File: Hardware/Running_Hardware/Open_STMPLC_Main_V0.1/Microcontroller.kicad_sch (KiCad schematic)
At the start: 73 parts, among them J1 Conn_02x08_Odd_Even, J12 USB C, J2 USB C, J3 Conn_01x04, SW1 Switch_6x6, U1 STM32F407IGTx, U3 TPS3430WDRC, U4 CH340C, Y1 48MHz, Y2 32.768kHz

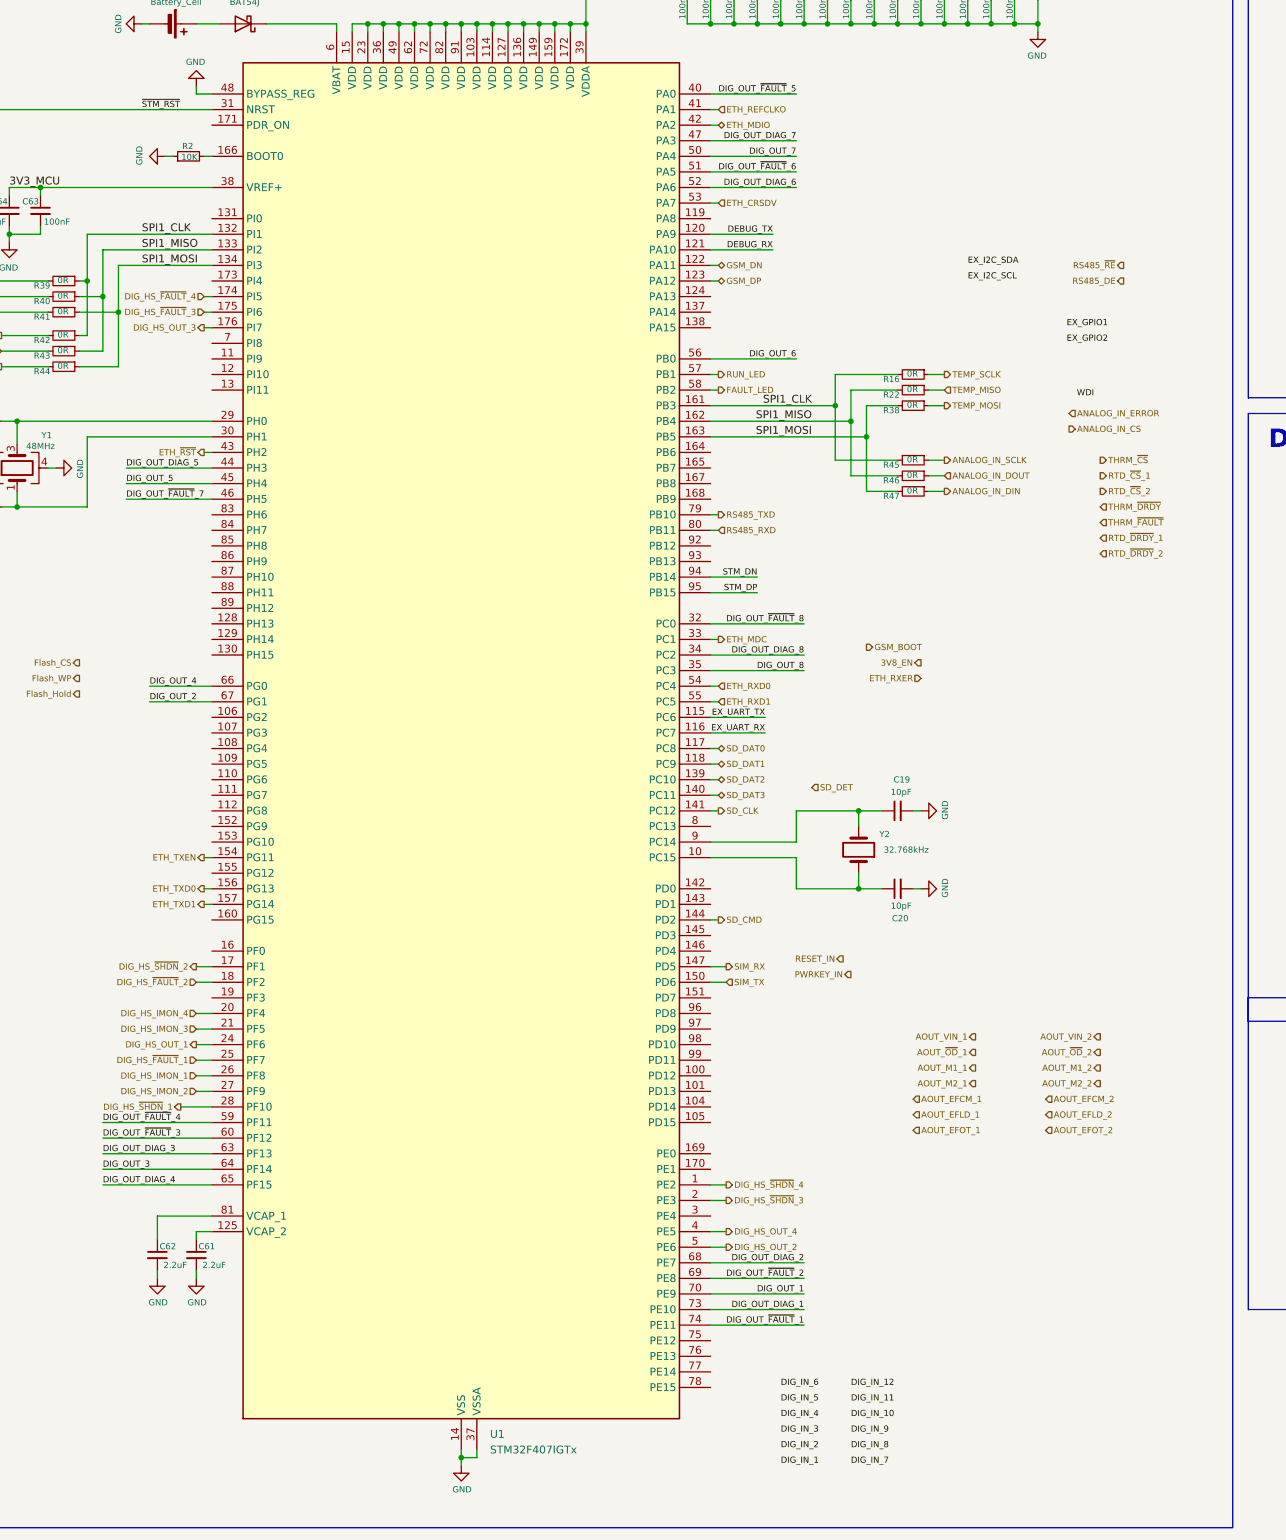
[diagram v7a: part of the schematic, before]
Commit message: Pin mapping
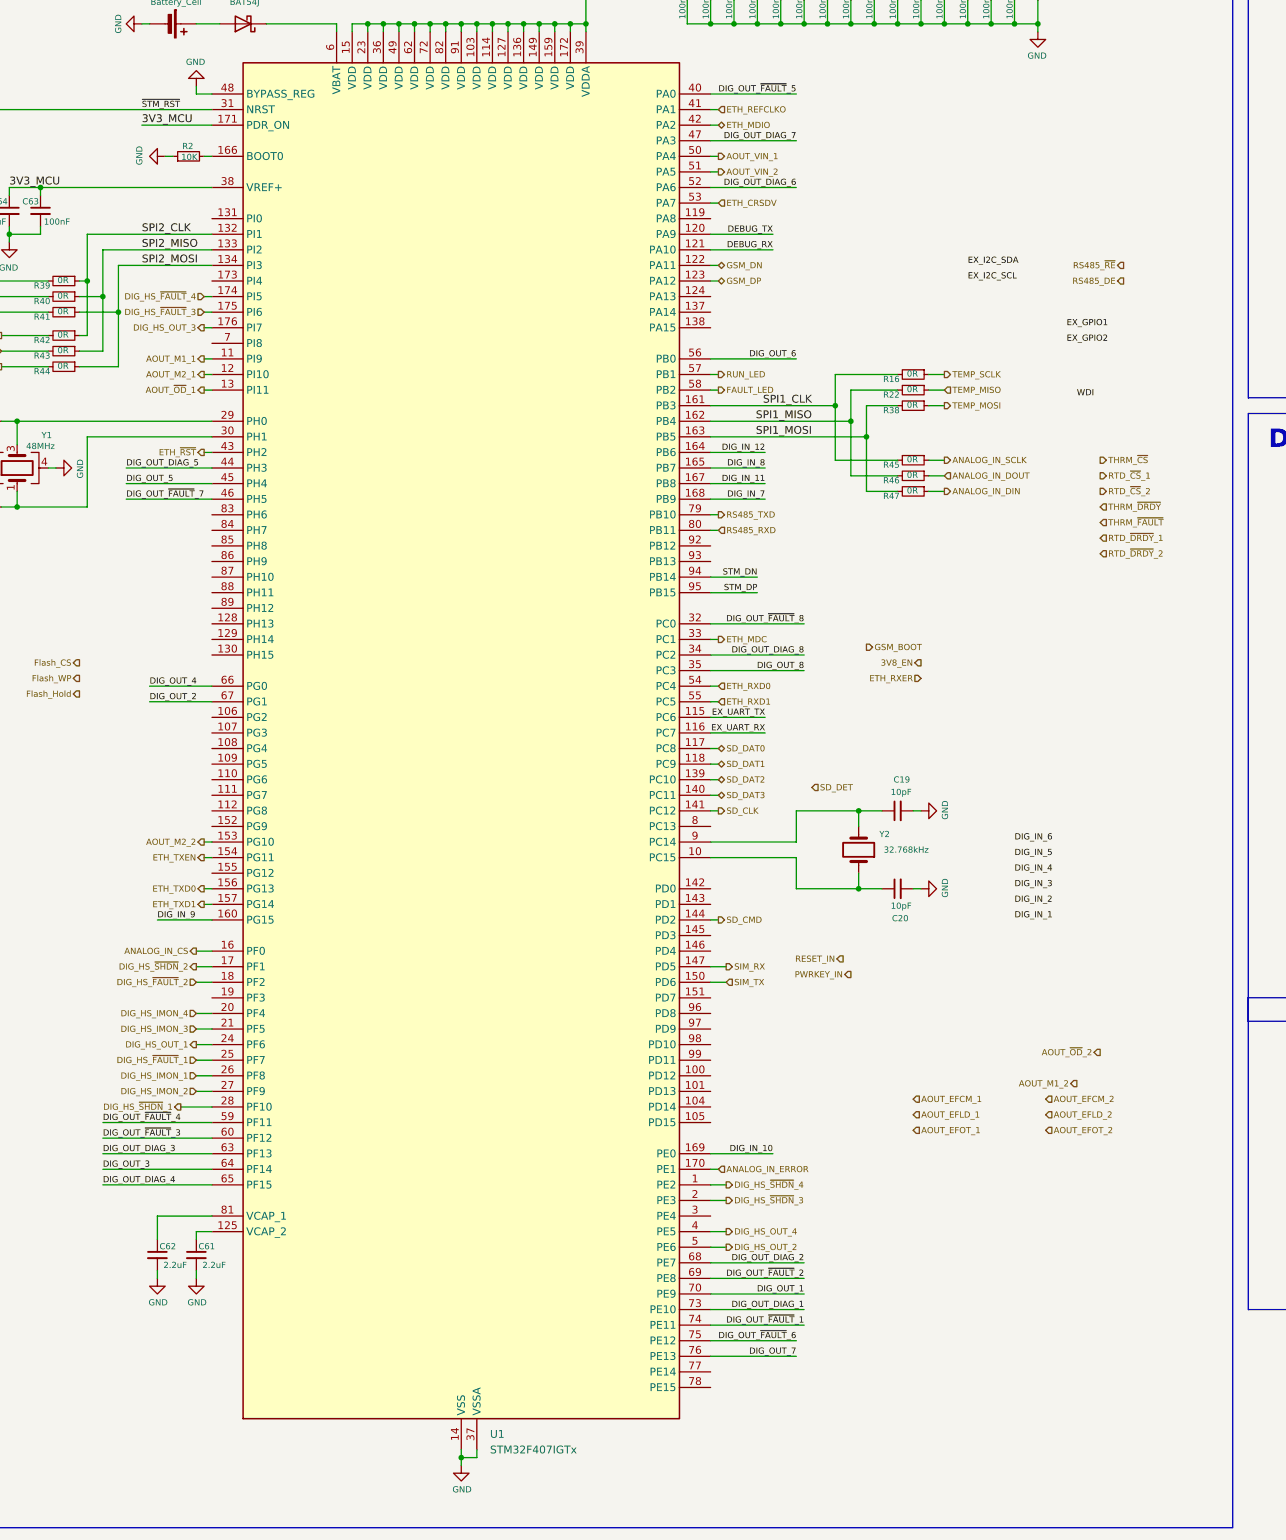
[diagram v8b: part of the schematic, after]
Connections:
- net 3V3_MCU: now also U1.171 (PDR_ON)
- net ANALOG_IN_CS: now also U1.16 (PF0)
- net ANALOG_IN_ERROR: now also U1.170 (PE1)
- net AOUT_M1_1: now also U1.11 (PI9)
- net AOUT_M2_1: now also U1.12 (PI10)
- net AOUT_M2_2: now also U1.153 (PG10)
- net AOUT_VIN_1: now also U1.50 (PA4)
- net AOUT_VIN_2: now also U1.51 (PA5)
- net AOUT_~{OD}_1: now also U1.13 (PI11)
- net DIG_IN_10: now also U1.169 (PE0)
- net DIG_IN_11: now also U1.167 (PB8)
- net DIG_IN_12: now also U1.164 (PB6)
- net DIG_IN_7: now also U1.168 (PB9)
- net DIG_IN_8: now also U1.165 (PB7)
- net DIG_IN_9: now also U1.160 (PG15)
- net DIG_OUT_7: now also U1.76 (PE13); no longer U1.50 (PA4)
- net DIG_OUT_~{FAULT}_6: now also U1.75 (PE12); no longer U1.51 (PA5)
- net SPI1_CLK: no longer R39.1, R42.1, U1.132 (PI1)
- net SPI1_MISO: no longer R40.1, R43.1, U1.133 (PI2)
- net SPI1_MOSI: no longer R41.1, R44.1, U1.134 (PI3)
- new net SPI2_CLK: R39.1, R42.1, U1.132 (PI1)
- new net SPI2_MISO: R40.1, R43.1, U1.133 (PI2)
- new net SPI2_MOSI: R41.1, R44.1, U1.134 (PI3)
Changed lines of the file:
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@@
 	(wire
 		(pts
+			(xy 66.04 170.18) (xy 67.31 170.18)
+		)
+		(stroke
+			(width 0)
+			(type default)
+		)
+	)
+	(wire
+		(pts
 			(xy 160.02 33.02) (xy 160.02 36.83)
 		)
@@
 	(wire
 		(pts
+			(xy 66.04 91.44) (xy 67.31 91.44)
+		)
+		(stroke
+			(width 0)
+			(type default)
+		)
+	)
+	(wire
+		(pts
 			(xy 184.15 110.49) (xy 186.69 110.49)
 		)
@@
 	(wire
 		(pts
+			(xy 66.04 96.52) (xy 67.31 96.52)
+		)
+		(stroke
+			(width 0)
+			(type default)
+		)
+	)
+	(wire
+		(pts
 			(xy 95.25 36.83) (xy 97.79 36.83)
 		)
@@
 	(wire
 		(pts
+			(xy 58.42 182.88) (xy 67.31 182.88)
+		)
+		(stroke
+			(width 0)
+			(type default)
+		)
+	)
+	(wire
+		(pts
 			(xy 309.88 200.66) (xy 309.88 214.63)
 		)
@@
 	(wire
 		(pts
+			(xy 148.59 220.98) (xy 158.75 220.98)
+		)
+		(stroke
+			(width 0)
+			(type default)
+		)
+	)
+	(wire
+		(pts
 			(xy 260.35 41.91) (xy 260.35 46.99)
 		)
@@
 	(wire
 		(pts
+			(xy 66.04 93.98) (xy 67.31 93.98)
+		)
+		(stroke
+			(width 0)
+			(type default)
+		)
+	)
+	(wire
+		(pts
 			(xy 29.21 109.22) (xy 30.48 109.22)
 		)
@@
 	(wire
 		(pts
+			(xy 148.59 109.22) (xy 157.48 109.22)
+		)
+		(stroke
+			(width 0)
+			(type default)
+		)
+	)
+	(wire
+		(pts
 			(xy 167.64 33.02) (xy 167.64 36.83)
 		)
@@
 	(wire
 		(pts
+			(xy 148.59 60.96) (xy 149.86 60.96)
+		)
+		(stroke
+			(width 0)
+			(type default)
+		)
+	)
+	(wire
+		(pts
 			(xy 49.53 218.44) (xy 67.31 218.44)
 		)
@@
 	(wire
 		(pts
+			(xy 64.77 187.96) (xy 67.31 187.96)
+		)
+		(stroke
+			(width 0)
+			(type default)
+		)
+	)
+	(wire
+		(pts
 			(xy 148.59 144.78) (xy 149.86 144.78)
 		)
@@
 	(wire
 		(pts
+			(xy 149.86 58.42) (xy 148.59 58.42)
+		)
+		(stroke
+			(width 0)
+			(type default)
+		)
+	)
+	(wire
+		(pts
 			(xy 179.07 25.4) (xy 179.07 27.94)
 		)
@@
 	(wire
 		(pts
+			(xy 55.88 53.34) (xy 67.31 53.34)
+		)
+		(stroke
+			(width 0)
+			(type default)
+		)
+	)
+	(wire
+		(pts
 			(xy 66.04 177.8) (xy 67.31 177.8)
 		)
@@
 	(wire
 		(pts
-			(xy 148.59 58.42) (xy 162.56 58.42)
+			(xy 148.59 254) (xy 162.56 254)
 		)
 		(stroke
@@
 	(wire
 		(pts
+			(xy 149.86 223.52) (xy 148.59 223.52)
+		)
+		(stroke
+			(width 0)
+			(type default)
+		)
+	)
+	(wire
+		(pts
 			(xy 291.465 120.65) (xy 291.465 124.46)
 		)
@@
 	(wire
 		(pts
+			(xy 148.59 114.3) (xy 157.48 114.3)
+		)
+		(stroke
+			(width 0)
+			(type default)
+		)
+	)
+	(wire
+		(pts
 			(xy 148.59 127) (xy 156.21 127)
 		)
@@
 		)
 	)
+	(wire
+		(pts
+			(xy 148.59 111.76) (xy 157.48 111.76)
+		)
+		(stroke
+			(width 0)
+			(type default)
+		)
+	)
 	(bus
 		(pts
@@
 	(wire
 		(pts
-			(xy 148.59 60.96) (xy 162.56 60.96)
+			(xy 148.59 251.46) (xy 162.56 251.46)
 		)
 		(stroke
@@
 		)
 	)
+	(wire
+		(pts
+			(xy 148.59 106.68) (xy 157.48 106.68)
+		)
+		(stroke
+			(width 0)
+			(type default)
+		)
+	)
 	(bus
 		(pts
@@
 	)
 	(label "DIG_IN_2"
-		(at 160.02 269.24 0)
+		(at 198.12 180.34 0)
 		(effects
 			(font
@@
 	)
 	(label "DIG_IN_3"
-		(at 160.02 266.7 0)
+		(at 198.12 177.8 0)
 		(effects
 			(font
@@
 	)
 	(label "DIG_IN_10"
-		(at 171.45 264.16 0)
+		(at 158.75 220.98 180)
 		(effects
 			(font
 				(size 1 1)
 			)
-			(justify left bottom)
+			(justify right bottom)
 		)
 	)
@@
 	)
 	(label "DIG_IN_1"
-		(at 160.02 271.78 0)
+		(at 198.12 182.88 0)
 		(effects
 			(font
@@
 	)
 	(label "DIG_IN_12"
-		(at 171.45 259.08 0)
+		(at 157.48 106.68 180)
 		(effects
 			(font
 				(size 1 1)
 			)
-			(justify left bottom)
+			(justify right bottom)
 		)
 	)
@@
 	)
 	(label "DIG_OUT_~{FAULT}_6"
-		(at 162.56 60.96 180)
+		(at 162.56 251.46 180)
 		(effects
 			(font
@@
 	)
 	(label "DIG_IN_5"
-		(at 160.02 261.62 0)
+		(at 198.12 172.72 0)
 		(effects
 			(font
@@
 	)
 	(label "DIG_IN_8"
-		(at 171.45 269.24 0)
+		(at 157.48 109.22 180)
 		(effects
 			(font
 				(size 1 1)
 			)
-			(justify left bottom)
+			(justify right bottom)
 		)
 	)
@@
 	)
 	(label "DIG_IN_4"
-		(at 160.02 264.16 0)
+		(at 198.12 175.26 0)
 		(effects
 			(font
@@
 	)
 	(label "DIG_IN_6"
-		(at 160.02 259.08 0)
+		(at 198.12 170.18 0)
 		(effects
 			(font
@@
 		)
 	)
-	(label "SPI1_MOSI"
+	(label "3V3_MCU"
+		(at 55.88 53.34 0)
+		(effects
+			(font
+				(size 1.27 1.27)
+			)
+			(justify left bottom)
+		)
+	)
+	(label "SPI2_MOSI"
 		(at 55.88 76.2 0)
 		(effects
@@
 		)
 	)
-	(label "SPI1_CLK"
+	(label "SPI2_CLK"
 		(at 55.88 71.12 0)
 		(effects
@@
 	)
 	(label "DIG_IN_7"
-		(at 171.45 271.78 0)
+		(at 157.48 114.3 180)
 		(effects
 			(font
 				(size 1 1)
 			)
-			(justify left bottom)
+			(justify right bottom)
 		)
 	)
@@
 		)
 	)
-	(label "SPI1_MISO"
+	(label "SPI2_MISO"
 		(at 55.88 73.66 0)
 		(effects
@@
 	)
 	(label "DIG_IN_9"
-		(at 171.45 266.7 0)
+		(at 58.42 182.88 0)
 		(effects
 			(font
@@
 	)
 	(label "DIG_OUT_7"
-		(at 162.56 58.42 180)
+		(at 162.56 254 180)
 		(effects
 			(font
@@
 	)
 	(label "DIG_IN_11"
-		(at 171.45 261.62 0)
+		(at 157.48 111.76 180)
 		(effects
 			(font
 				(size 1 1)
 			)
-			(justify left bottom)
+			(justify right bottom)
 		)
 	)
@@
 	(hierarchical_label "ANALOG_IN_CS"
 		(shape output)
-		(at 207.01 102.87 0)
+		(at 64.77 187.96 180)
 		(effects
 			(font
 				(size 1 1)
 			)
-			(justify left)
+			(justify right)
 		)
 	)
 	(hierarchical_label "AOUT_VIN_1"
 		(shape output)
-		(at 191.77 201.93 180)
+		(at 149.86 58.42 0)
 		(effects
 			(font
 				(size 1 1)
 			)
-			(justify right)
+			(justify left)
 		)
 	)
 	(hierarchical_label "AOUT_VIN_2"
 		(shape output)
-		(at 212.09 201.93 180)
+		(at 149.86 60.96 0)
 		(effects
 			(font
 				(size 1 1)
 			)
-			(justify right)
+			(justify left)
 		)
 	)
@@
 	(hierarchical_label "AOUT_~{OD}_1"
 		(shape output)
-		(at 191.77 204.47 180)
+		(at 66.04 96.52 180)
 		(effects
 			(font
@@
 	(hierarchical_label "ANALOG_IN_ERROR"
 		(shape input)
-		(at 207.01 100.33 0)
+		(at 149.86 223.52 0)
 		(effects
 			(font
@@
 	(hierarchical_label "AOUT_M2_1"
 		(shape output)
-		(at 191.77 209.55 180)
+		(at 66.04 93.98 180)
 		(effects
 			(font
@@
 	(hierarchical_label "AOUT_M2_2"
 		(shape output)
-		(at 212.09 209.55 180)
+		(at 66.04 170.18 180)
 		(effects
 			(font
@@
 	(hierarchical_label "AOUT_M1_2"
 		(shape output)
-		(at 212.09 207.01 180)
+		(at 208.28 209.55 180)
 		(effects
 			(font
@@
 	(hierarchical_label "AOUT_M1_1"
 		(shape output)
-		(at 191.77 207.01 180)
+		(at 66.04 91.44 180)
 		(effects
 			(font
